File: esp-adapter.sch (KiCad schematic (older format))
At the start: 4 parts, among them J1 Conn_01x11_Male, J2 Conn_01x11_Male, J3 Conn_01x02_Male, U1 ESP-07

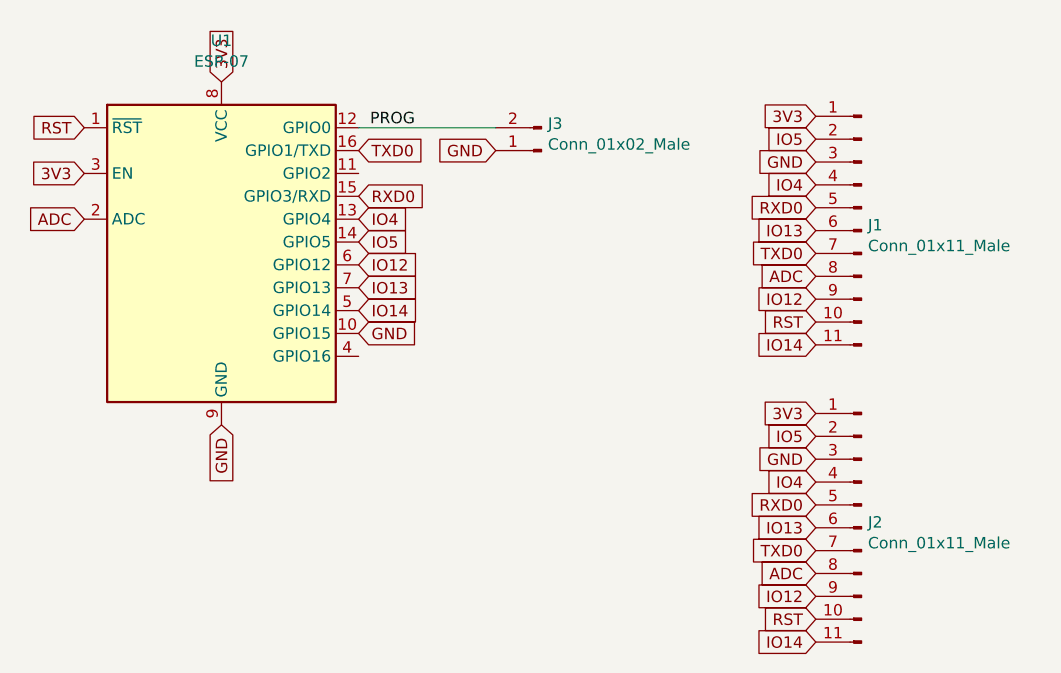
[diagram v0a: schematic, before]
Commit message: fix TX RX swap
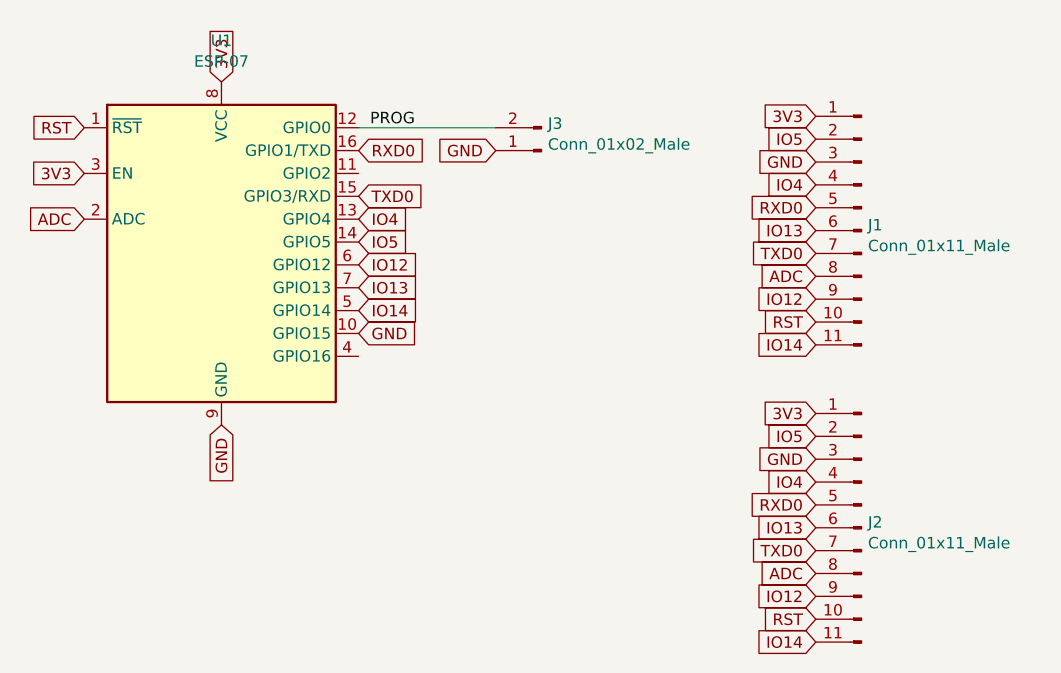
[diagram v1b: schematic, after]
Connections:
- net RXD0: now also U1.16 (GPIO1/TXD); no longer U1.15 (GPIO3/RXD)
- net TXD0: now also U1.15 (GPIO3/RXD); no longer U1.16 (GPIO1/TXD)
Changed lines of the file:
@@
 Text GLabel 6000 4000 3    50   Input ~ 0
 GND
+Text GLabel 6600 3000 2    50   Input ~ 0
+TXD0
 Text GLabel 6600 2800 2    50   Input ~ 0
-TXD0
-Text GLabel 6600 3000 2    50   Input ~ 0
 RXD0
 Text GLabel 6600 3200 2    50   Input ~ 0

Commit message: Revert "fix TX RX swap"
This reverts commit 031c61bf6d1d21104408cedd763a9be0f04462ce.
For explanation see issue #2 .
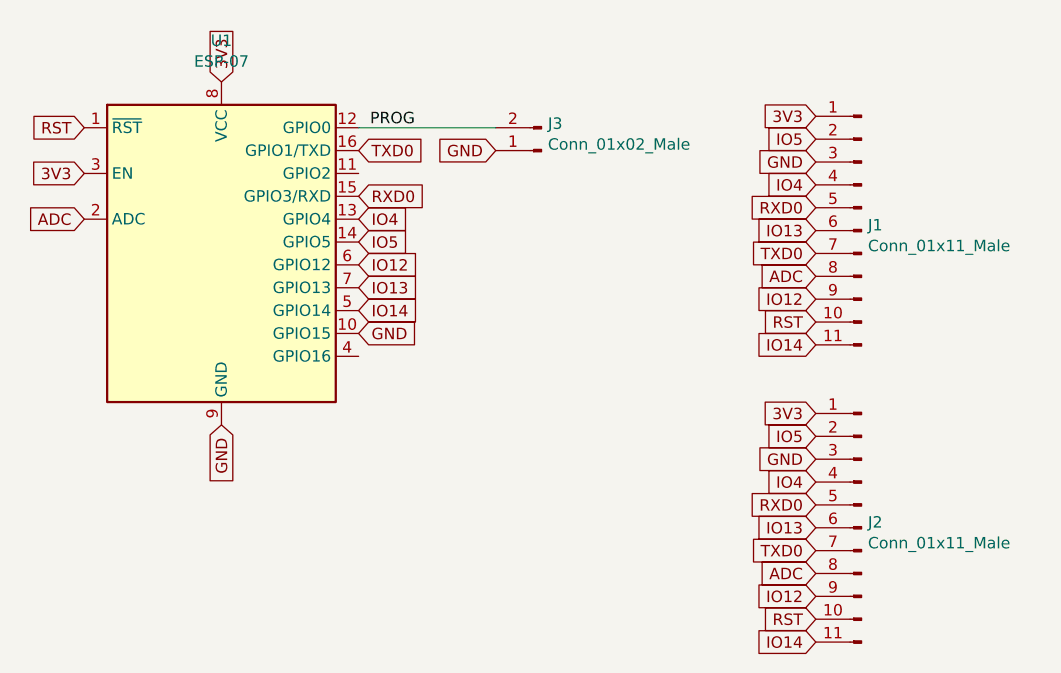
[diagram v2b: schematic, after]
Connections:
- net RXD0: now also U1.15 (GPIO3/RXD); no longer U1.16 (GPIO1/TXD)
- net TXD0: now also U1.16 (GPIO1/TXD); no longer U1.15 (GPIO3/RXD)
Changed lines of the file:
@@
 Text GLabel 6000 4000 3    50   Input ~ 0
 GND
+Text GLabel 6600 2800 2    50   Input ~ 0
+TXD0
 Text GLabel 6600 3000 2    50   Input ~ 0
-TXD0
-Text GLabel 6600 2800 2    50   Input ~ 0
 RXD0
 Text GLabel 6600 3200 2    50   Input ~ 0
